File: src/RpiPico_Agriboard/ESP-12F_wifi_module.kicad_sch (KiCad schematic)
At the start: 12 parts, among them J27 Conn_02x05_Odd_Even, SW3 SW_Push, SW4 SW_Push, U4 ESP-12F

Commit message: schematic updates completed
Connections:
- net +3V3: no longer C21.1, R15.1, R16.1, R29.1, U4.8 (VCC)
- new net MODULES_PWR_3V3: C21.1, R15.1, R16.1, R29.1, U4.8 (VCC)
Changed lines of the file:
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@@
-    (stroke (width 0) (type default))
-  )
-  (wire (pts (xy 170.815 45.72) (xy 170.815 48.26))
     (stroke (width 0) (type default))
   )
@@
     (effects (font (size 1.27 1.27)) (justify left bottom))
   )
+  (global_label "MODULES_PWR_3V3" (shape input) (at 100.965 52.705 90) (fields_autoplaced)
+    (effects (font (size 0.8 0.8)) (justify left))
+    (property "Intersheetrefs" "${INTERSHEET_REFS}" (at 100.965 39.4081 90)
+      (effects (font (size 1.27 1.27)) (justify left) hide)
+    )
+  )
+  (global_label "MODULES_PWR_3V3" (shape input) (at 170.815 48.26 90) (fields_autoplaced)
+    (effects (font (size 0.8 0.8)) (justify left))
+    (property "Intersheetrefs" "${INTERSHEET_REFS}" (at 170.815 34.9631 90)
+      (effects (font (size 1.27 1.27)) (justify left) hide)
+    )
+  )
+  (global_label "MODULES_PWR_3V3" (shape input) (at 139.7 50.165 90) (fields_autoplaced)
+    (effects (font (size 0.8 0.8)) (justify left))
+    (property "Intersheetrefs" "${INTERSHEET_REFS}" (at 139.7 36.8681 90)
+      (effects (font (size 1.27 1.27)) (justify left) hide)
+    )
+  )
+  (global_label "MODULES_PWR_3V3" (shape input) (at 108.585 52.705 90) (fields_autoplaced)
+    (effects (font (size 0.8 0.8)) (justify left))
+    (property "Intersheetrefs" "${INTERSHEET_REFS}" (at 108.585 39.4081 90)
+      (effects (font (size 1.27 1.27)) (justify left) hide)
+    )
+  )
   (hierarchical_label "ESP8266_RX_out" (shape input) (at 217.17 106.045 0) (fields_autoplaced)
     (effects (font (size 1.27 1.27) bold) (justify left))
@@
   (hierarchical_label "ESP8266_TX_out" (shape input) (at 217.17 100.965 0) (fields_autoplaced)
     (effects (font (size 1.27 1.27) bold) (justify left))
-  )
-  (symbol (lib_id "power:+3V3") (at 108.585 52.705 0) (unit 1)
-    (in_bom yes) (on_board yes) (dnp no) (fields_autoplaced)
-    (property "Reference" "#PWR040" (at 108.585 56.515 0)
-      (effects (font (size 1.27 1.27)) hide)
-    )
-    (property "Value" "+3V3" (at 108.585 47.625 0)
-      (effects (font (size 1.27 1.27)))
-    )
-    (property "Footprint" "" (at 108.585 52.705 0)
-      (effects (font (size 1.27 1.27)) hide)
-    )
-    (property "Datasheet" "" (at 108.585 52.705 0)
-      (effects (font (size 1.27 1.27)) hide)
-    )
-    (pin "1")
-    (instances
-      (project "RpiPico_Agriboard"
-        (path "/c2474b65-c0e8-4987-86b2-fddddd4113dc/24a6f6dd-59ed-4a3f-ab3f-0a381255370f/72a22278-332d-4fac-9f87-e146604ac9df"
-          (reference "#PWR040") (unit 1)
-        )
-      )
-    )
-  )
-  (symbol (lib_id "power:+3V3") (at 100.965 52.705 0) (unit 1)
-    (in_bom yes) (on_board yes) (dnp no) (fields_autoplaced)
-    (property "Reference" "#PWR039" (at 100.965 56.515 0)
-      (effects (font (size 1.27 1.27)) hide)
-    )
-    (property "Value" "+3V3" (at 100.965 47.625 0)
-      (effects (font (size 1.27 1.27)))
-    )
-    (property "Footprint" "" (at 100.965 52.705 0)
-      (effects (font (size 1.27 1.27)) hide)
-    )
-    (property "Datasheet" "" (at 100.965 52.705 0)
-      (effects (font (size 1.27 1.27)) hide)
-    )
-    (pin "1")
-    (instances
-      (project "RpiPico_Agriboard"
-        (path "/c2474b65-c0e8-4987-86b2-fddddd4113dc/24a6f6dd-59ed-4a3f-ab3f-0a381255370f/72a22278-332d-4fac-9f87-e146604ac9df"
-          (reference "#PWR039") (unit 1)
-        )
-      )
-    )
   )
   (symbol (lib_id "Device:R_US") (at 108.585 61.595 0) (unit 1)
@@
         (path "/c2474b65-c0e8-4987-86b2-fddddd4113dc/24a6f6dd-59ed-4a3f-ab3f-0a381255370f/72a22278-332d-4fac-9f87-e146604ac9df"
           (reference "TP_rx1") (unit 1)
-        )
-      )
-    )
-  )
-  (symbol (lib_id "power:+3V3") (at 139.7 50.165 0) (unit 1)
-    (in_bom yes) (on_board yes) (dnp no) (fields_autoplaced)
-    (property "Reference" "#PWR041" (at 139.7 53.975 0)
-      (effects (font (size 1.27 1.27)) hide)
-    )
-    (property "Value" "+3V3" (at 139.7 45.085 0)
-      (effects (font (size 1.27 1.27)))
-    )
-    (property "Footprint" "" (at 139.7 50.165 0)
-      (effects (font (size 1.27 1.27)) hide)
-    )
-    (property "Datasheet" "" (at 139.7 50.165 0)
-      (effects (font (size 1.27 1.27)) hide)
-    )
-    (pin "1")
-    (instances
-      (project "RpiPico_Agriboard"
-        (path "/c2474b65-c0e8-4987-86b2-fddddd4113dc/24a6f6dd-59ed-4a3f-ab3f-0a381255370f/72a22278-332d-4fac-9f87-e146604ac9df"
-          (reference "#PWR041") (unit 1)
         )
       )
@@
         )
       )
-    )
-  )
-  (symbol (lib_id "power:+3V3") (at 170.815 45.72 0) (unit 1)
-    (in_bom yes) (on_board yes) (dnp no) (fields_autoplaced)
-    (property "Reference" "#PWR043" (at 170.815 49.53 0)
-      (effects (font (size 1.27 1.27)) hide)
-    )
-    (property "Value" "+3V3" (at 170.815 40.64 0)
-      (effects (font (size 1.27 1.27)))
-    )
-    (property "Footprint" "" (at 170.815 45.72 0)
-      (effects (font (size 1.27 1.27)) hide)
-    )
-    (property "Datasheet" "" (at 170.815 45.72 0)
-      (effects (font (size 1.27 1.27)) hide)
-    )
-    (pin "1")
-    (instances
-      (project "RpiPico_Agriboard"
-        (path "/c2474b65-c0e8-4987-86b2-fddddd4113dc/24a6f6dd-59ed-4a3f-ab3f-0a381255370f/72a22278-332d-4fac-9f87-e146604ac9df"
-          (reference "#PWR043") (unit 1)
-        )
-      )

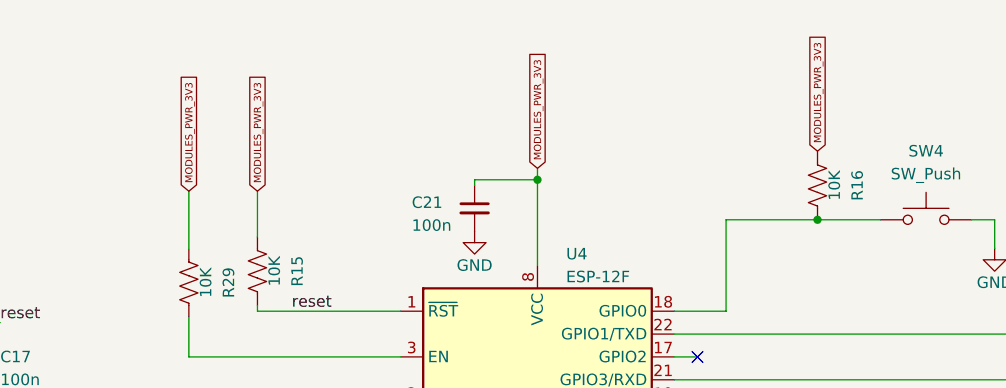
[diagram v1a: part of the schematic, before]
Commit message: Revert "schematic updates completed"
This reverts commit 0124993096667d53f20fd59dec80d3f5a1efcd43.
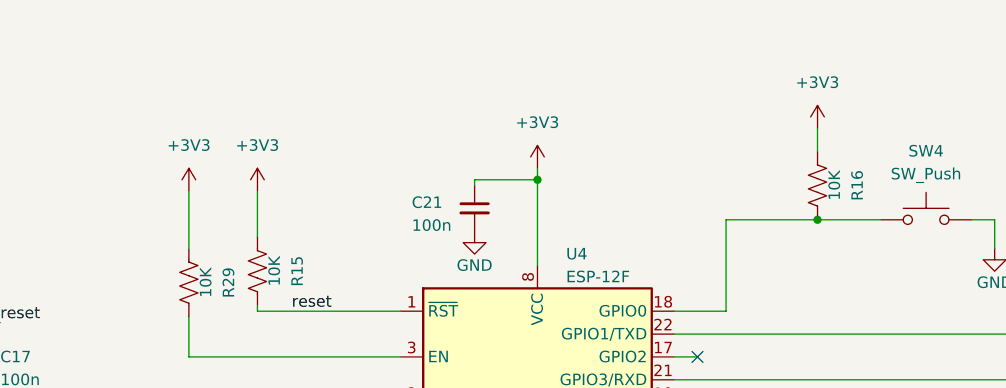
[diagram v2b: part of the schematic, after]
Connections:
- net MODULES_PWR_3V3 is gone; now on net +3V3: C21.1, R15.1, R16.1, R29.1, U4.8 (VCC)
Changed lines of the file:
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@@
+    (stroke (width 0) (type default))
+  )
+  (wire (pts (xy 170.815 45.72) (xy 170.815 48.26))
     (stroke (width 0) (type default))
   )
@@
     (effects (font (size 1.27 1.27)) (justify left bottom))
   )
-  (global_label "MODULES_PWR_3V3" (shape input) (at 100.965 52.705 90) (fields_autoplaced)
-    (effects (font (size 0.8 0.8)) (justify left))
-    (property "Intersheetrefs" "${INTERSHEET_REFS}" (at 100.965 39.4081 90)
-      (effects (font (size 1.27 1.27)) (justify left) hide)
-    )
-  )
-  (global_label "MODULES_PWR_3V3" (shape input) (at 170.815 48.26 90) (fields_autoplaced)
-    (effects (font (size 0.8 0.8)) (justify left))
-    (property "Intersheetrefs" "${INTERSHEET_REFS}" (at 170.815 34.9631 90)
-      (effects (font (size 1.27 1.27)) (justify left) hide)
-    )
-  )
-  (global_label "MODULES_PWR_3V3" (shape input) (at 139.7 50.165 90) (fields_autoplaced)
-    (effects (font (size 0.8 0.8)) (justify left))
-    (property "Intersheetrefs" "${INTERSHEET_REFS}" (at 139.7 36.8681 90)
-      (effects (font (size 1.27 1.27)) (justify left) hide)
-    )
-  )
-  (global_label "MODULES_PWR_3V3" (shape input) (at 108.585 52.705 90) (fields_autoplaced)
-    (effects (font (size 0.8 0.8)) (justify left))
-    (property "Intersheetrefs" "${INTERSHEET_REFS}" (at 108.585 39.4081 90)
-      (effects (font (size 1.27 1.27)) (justify left) hide)
-    )
-  )
   (hierarchical_label "ESP8266_RX_out" (shape input) (at 217.17 106.045 0) (fields_autoplaced)
     (effects (font (size 1.27 1.27) bold) (justify left))
@@
     (effects (font (size 1.27 1.27) bold) (justify left))
   )
+  (symbol (lib_id "power:+3V3") (at 108.585 52.705 0) (unit 1)
+    (in_bom yes) (on_board yes) (dnp no) (fields_autoplaced)
+    (property "Reference" "#PWR040" (at 108.585 56.515 0)
+      (effects (font (size 1.27 1.27)) hide)
+    )
+    (property "Value" "+3V3" (at 108.585 47.625 0)
+      (effects (font (size 1.27 1.27)))
+    )
+    (property "Footprint" "" (at 108.585 52.705 0)
+      (effects (font (size 1.27 1.27)) hide)
+    )
+    (property "Datasheet" "" (at 108.585 52.705 0)
+      (effects (font (size 1.27 1.27)) hide)
+    )
+    (pin "1")
+    (instances
+      (project "RpiPico_Agriboard"
+        (path "/c2474b65-c0e8-4987-86b2-fddddd4113dc/24a6f6dd-59ed-4a3f-ab3f-0a381255370f/72a22278-332d-4fac-9f87-e146604ac9df"
+          (reference "#PWR040") (unit 1)
+        )
+      )
+    )
+  )
+  (symbol (lib_id "power:+3V3") (at 100.965 52.705 0) (unit 1)
+    (in_bom yes) (on_board yes) (dnp no) (fields_autoplaced)
+    (property "Reference" "#PWR039" (at 100.965 56.515 0)
+      (effects (font (size 1.27 1.27)) hide)
+    )
+    (property "Value" "+3V3" (at 100.965 47.625 0)
+      (effects (font (size 1.27 1.27)))
+    )
+    (property "Footprint" "" (at 100.965 52.705 0)
+      (effects (font (size 1.27 1.27)) hide)
+    )
+    (property "Datasheet" "" (at 100.965 52.705 0)
+      (effects (font (size 1.27 1.27)) hide)
+    )
+    (pin "1")
+    (instances
+      (project "RpiPico_Agriboard"
+        (path "/c2474b65-c0e8-4987-86b2-fddddd4113dc/24a6f6dd-59ed-4a3f-ab3f-0a381255370f/72a22278-332d-4fac-9f87-e146604ac9df"
+          (reference "#PWR039") (unit 1)
+        )
+      )
+    )
+  )
   (symbol (lib_id "Device:R_US") (at 108.585 61.595 0) (unit 1)
     (in_bom yes) (on_board yes) (dnp no)
@@
         (path "/c2474b65-c0e8-4987-86b2-fddddd4113dc/24a6f6dd-59ed-4a3f-ab3f-0a381255370f/72a22278-332d-4fac-9f87-e146604ac9df"
           (reference "TP_rx1") (unit 1)
+        )
+      )
+    )
+  )
+  (symbol (lib_id "power:+3V3") (at 139.7 50.165 0) (unit 1)
+    (in_bom yes) (on_board yes) (dnp no) (fields_autoplaced)
+    (property "Reference" "#PWR041" (at 139.7 53.975 0)
+      (effects (font (size 1.27 1.27)) hide)
+    )
+    (property "Value" "+3V3" (at 139.7 45.085 0)
+      (effects (font (size 1.27 1.27)))
+    )
+    (property "Footprint" "" (at 139.7 50.165 0)
+      (effects (font (size 1.27 1.27)) hide)
+    )
+    (property "Datasheet" "" (at 139.7 50.165 0)
+      (effects (font (size 1.27 1.27)) hide)
+    )
+    (pin "1")
+    (instances
+      (project "RpiPico_Agriboard"
+        (path "/c2474b65-c0e8-4987-86b2-fddddd4113dc/24a6f6dd-59ed-4a3f-ab3f-0a381255370f/72a22278-332d-4fac-9f87-e146604ac9df"
+          (reference "#PWR041") (unit 1)
         )
       )
@@
         )
       )
+    )
+  )
+  (symbol (lib_id "power:+3V3") (at 170.815 45.72 0) (unit 1)
+    (in_bom yes) (on_board yes) (dnp no) (fields_autoplaced)
+    (property "Reference" "#PWR043" (at 170.815 49.53 0)
+      (effects (font (size 1.27 1.27)) hide)
+    )
+    (property "Value" "+3V3" (at 170.815 40.64 0)
+      (effects (font (size 1.27 1.27)))
+    )
+    (property "Footprint" "" (at 170.815 45.72 0)
+      (effects (font (size 1.27 1.27)) hide)
+    )
+    (property "Datasheet" "" (at 170.815 45.72 0)
+      (effects (font (size 1.27 1.27)) hide)
+    )
+    (pin "1")
+    (instances
+      (project "RpiPico_Agriboard"
+        (path "/c2474b65-c0e8-4987-86b2-fddddd4113dc/24a6f6dd-59ed-4a3f-ab3f-0a381255370f/72a22278-332d-4fac-9f87-e146604ac9df"
+          (reference "#PWR043") (unit 1)
+        )
+      )
